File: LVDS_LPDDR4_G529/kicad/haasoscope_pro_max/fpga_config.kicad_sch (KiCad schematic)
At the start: 1 part, among them U3 Ti90G529_Functions

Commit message: Aligned schematics, sort of
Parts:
- removed U3: Ti90G529_Functions, G529:BGA-529_23x23_19.0x19.0mm, symbol Ti90G529_Functions:Ti90G529_Functions
- added U3: Ti90G529_Functions, haasoscope_pro_adc_fpga_board:BGA-529_23x23_19.0x19.0mm, symbol Ti90G529_Functions:Ti90G529_Functions

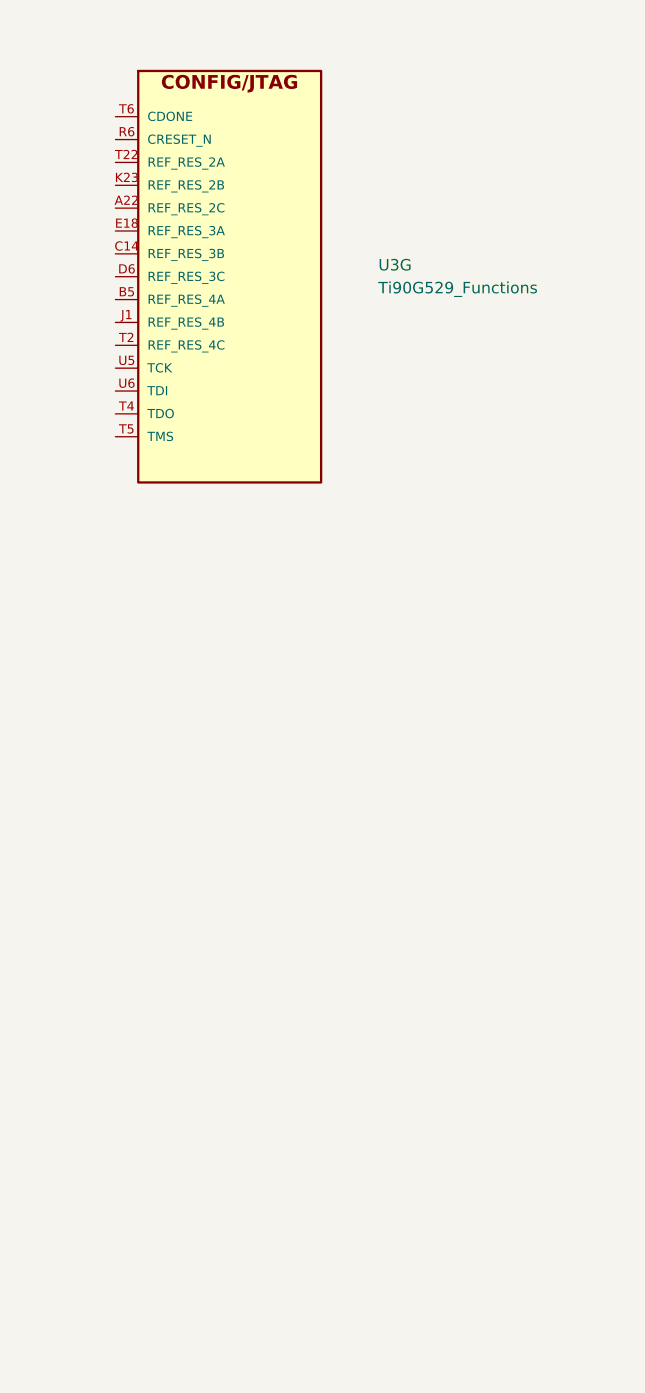
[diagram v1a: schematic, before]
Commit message: Aligned schematics, better
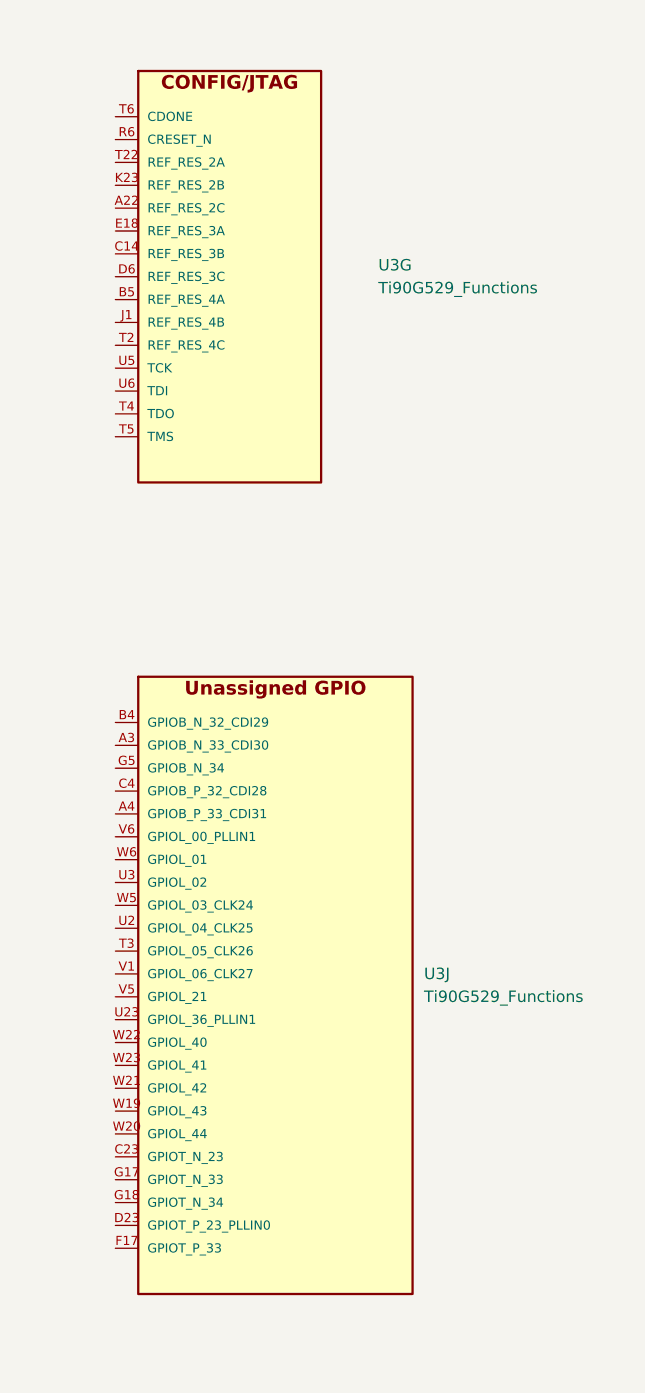
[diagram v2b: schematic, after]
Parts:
- added unit 10 of U3

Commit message: Aligned schematics, connected some components
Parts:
- U3: footprint haasoscope_pro_adc_fpga_board:BGA-529_23x23_19.0x19.0mm -> G529:BGA-529_23x23_19.0x19.0mm
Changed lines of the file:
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@@
 			)
 		)
-		(property "Footprint" "haasoscope_pro_adc_fpga_board:BGA-529_23x23_19.0x19.0mm"
+		(property "Footprint" "G529:BGA-529_23x23_19.0x19.0mm"
 			(at 146.05 134.62 0)
 			(effects
@@
 			)
 		)
-		(property "Footprint" "haasoscope_pro_adc_fpga_board:BGA-529_23x23_19.0x19.0mm"
+		(property "Footprint" "G529:BGA-529_23x23_19.0x19.0mm"
 			(at 146.05 55.88 0)
 			(effects

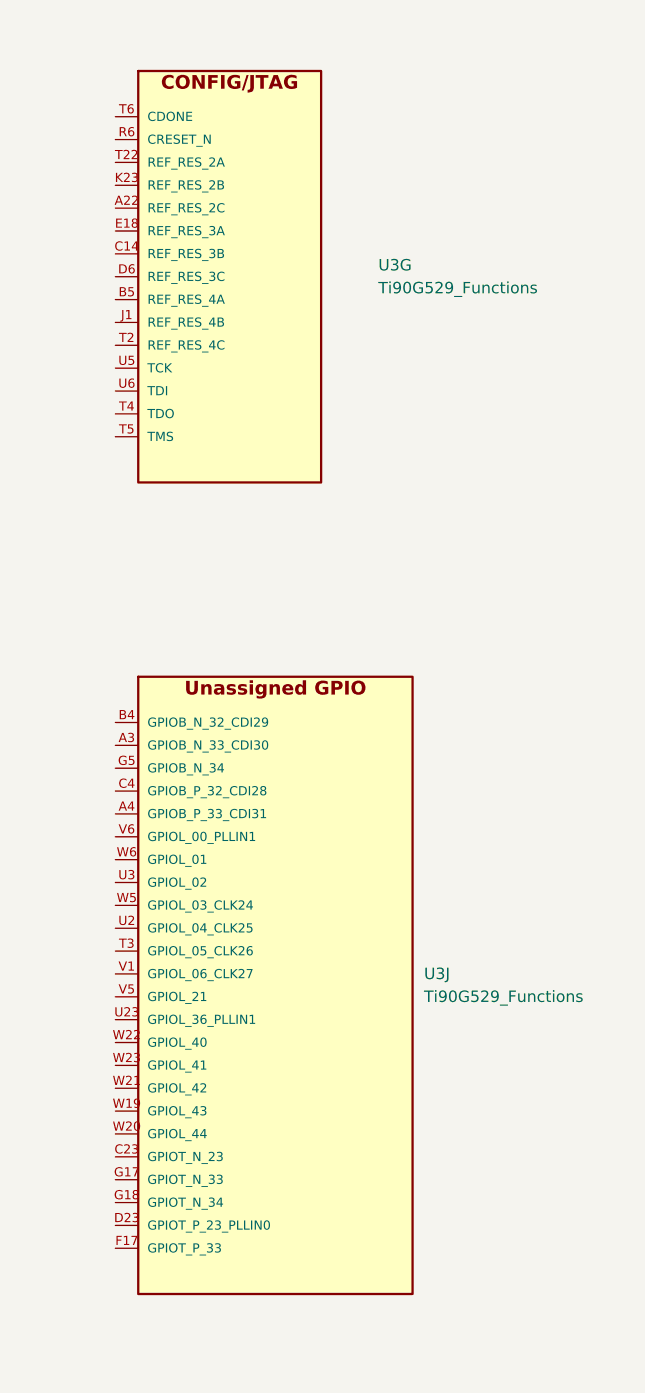
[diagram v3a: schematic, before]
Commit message: 6 NC pads
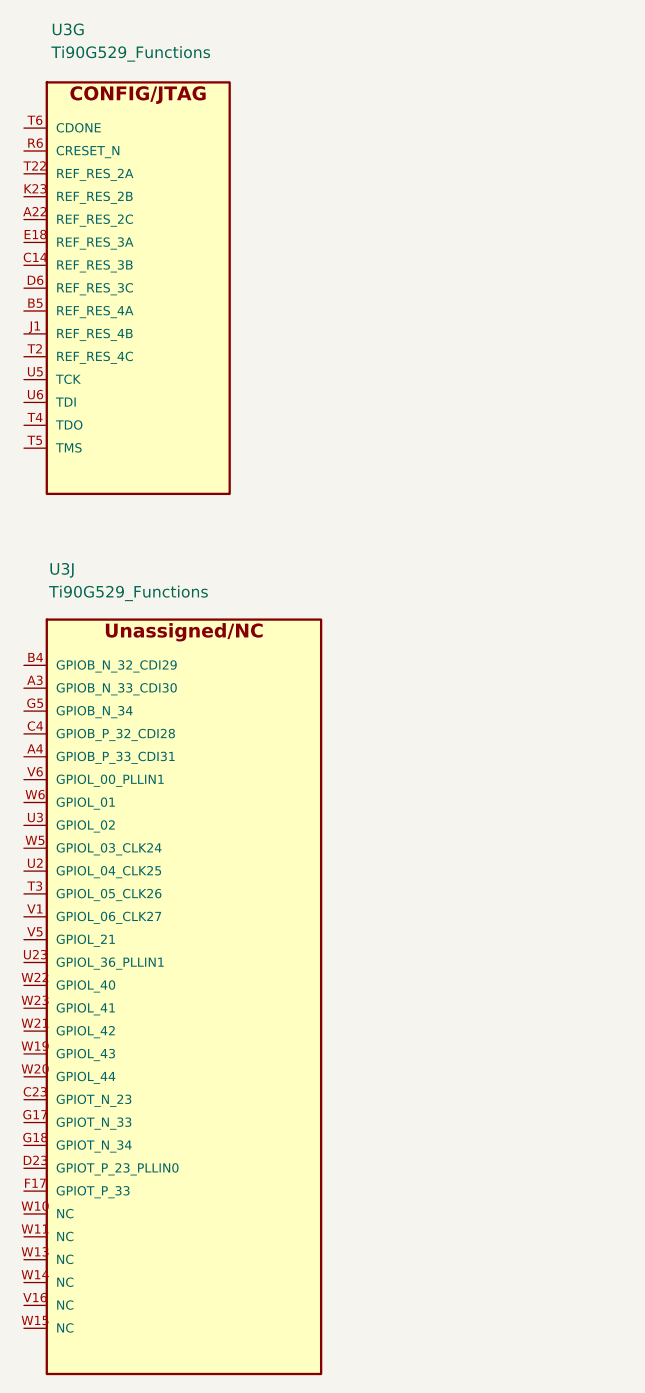
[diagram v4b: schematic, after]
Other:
- moved on the sheet: U3G
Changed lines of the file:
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@@
 	(symbol
 		(lib_id "Ti90G529_Functions:Ti90G529_Functions")
-		(at 146.05 130.81 0)
+		(at 135.89 132.08 0)
 		(unit 10)
 		(exclude_from_sim no)
@@
 		(on_board yes)
 		(dnp no)
-		(fields_autoplaced yes)
 		(property "Reference" "U3"
-			(at 177.8 129.5252 0)
+			(at 136.144 84.582 0)
 			(effects
 				(font
@@
 		)
 		(property "Value" "Ti90G529_Functions"
-			(at 177.8 132.0652 0)
+			(at 136.144 87.122 0)
 			(effects
 				(font
@@
 		)
 		(property "Footprint" "G529:BGA-529_23x23_19.0x19.0mm"
-			(at 146.05 134.62 0)
+			(at 135.89 135.89 0)
 			(effects
 				(font
@@
 		)
 		(property "Datasheet" ""
-			(at 146.05 137.16 0)
+			(at 135.89 138.43 0)
 			(effects
 				(font
@@
 		)
 		(property "Description" "Efinix Ti90G529 FPGA organized by peripheral interface"
-			(at 146.05 139.7 0)
+			(at 135.89 140.97 0)
 			(effects
 				(font
@@
 		)
 		(pin "D23"
+		)
+		(pin "V16"
+		)
+		(pin "W10"
+		)
+		(pin "W14"
+		)
+		(pin "W15"
+		)
+		(pin "W13"
+		)
+		(pin "W11"
 		)
 		(instances
@@
 	(symbol
 		(lib_id "Ti90G529_Functions:Ti90G529_Functions")
-		(at 146.05 52.07 0)
+		(at 135.89 53.34 0)
 		(unit 7)
 		(exclude_from_sim no)
@@
 		(on_board yes)
 		(dnp no)
-		(fields_autoplaced yes)
 		(property "Reference" "U3"
-			(at 172.72 50.7852 0)
+			(at 136.398 24.638 0)
 			(effects
 				(font
@@
 		)
 		(property "Value" "Ti90G529_Functions"
-			(at 172.72 53.3252 0)
+			(at 136.398 27.178 0)
 			(effects
 				(font
@@
 		)
 		(property "Footprint" "G529:BGA-529_23x23_19.0x19.0mm"
-			(at 146.05 55.88 0)
+			(at 135.89 57.15 0)
 			(effects
 				(font
@@
 		)
 		(property "Datasheet" ""
-			(at 146.05 58.42 0)
+			(at 135.89 59.69 0)
 			(effects
 				(font
@@
 		)
 		(property "Description" "Efinix Ti90G529 FPGA organized by peripheral interface"
-			(at 146.05 60.96 0)
+			(at 135.89 62.23 0)
 			(effects
 				(font
@@
 		(pin "D23"
 		)
+		(pin "W15"
+		)
+		(pin "W10"
+		)
+		(pin "W11"
+		)
+		(pin "W14"
+		)
+		(pin "V16"
+		)
+		(pin "W13"
+		)
 		(instances
